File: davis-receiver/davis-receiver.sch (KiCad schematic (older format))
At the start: 150 parts, among them J1 Conn_Coaxial, J2 Wurth_74982104400, J3 JTAG, J4 UART, J5 SPI-BARO, J6 SPI-RF, Q1 FDC2512, SW1 MCU_RESET, T1 POE70P-33, U1 TM4C129ENCZADI3R, U2 CC1125RHBR, U3 FXPS7115D4, U4 TPS79930DDCR, U5 MB10S, U6 MB10S, U7 TPS23753A, U8 FOD817A3SD, U9 TLV431ACDBZR, X1 ECS-2520MV-400-AY-TR, Y1 LFXTAL071758CUTT

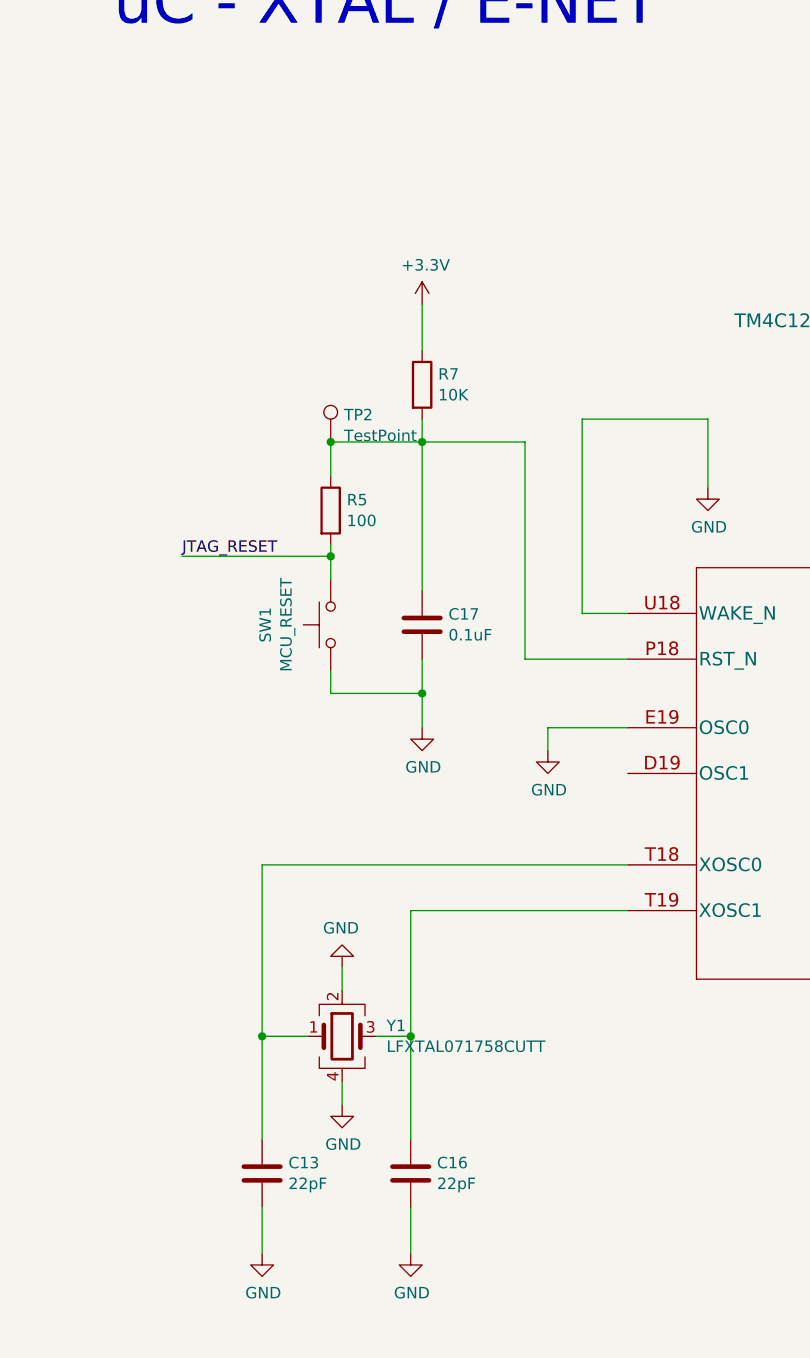
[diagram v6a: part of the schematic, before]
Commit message: Sea LED Routing Complete
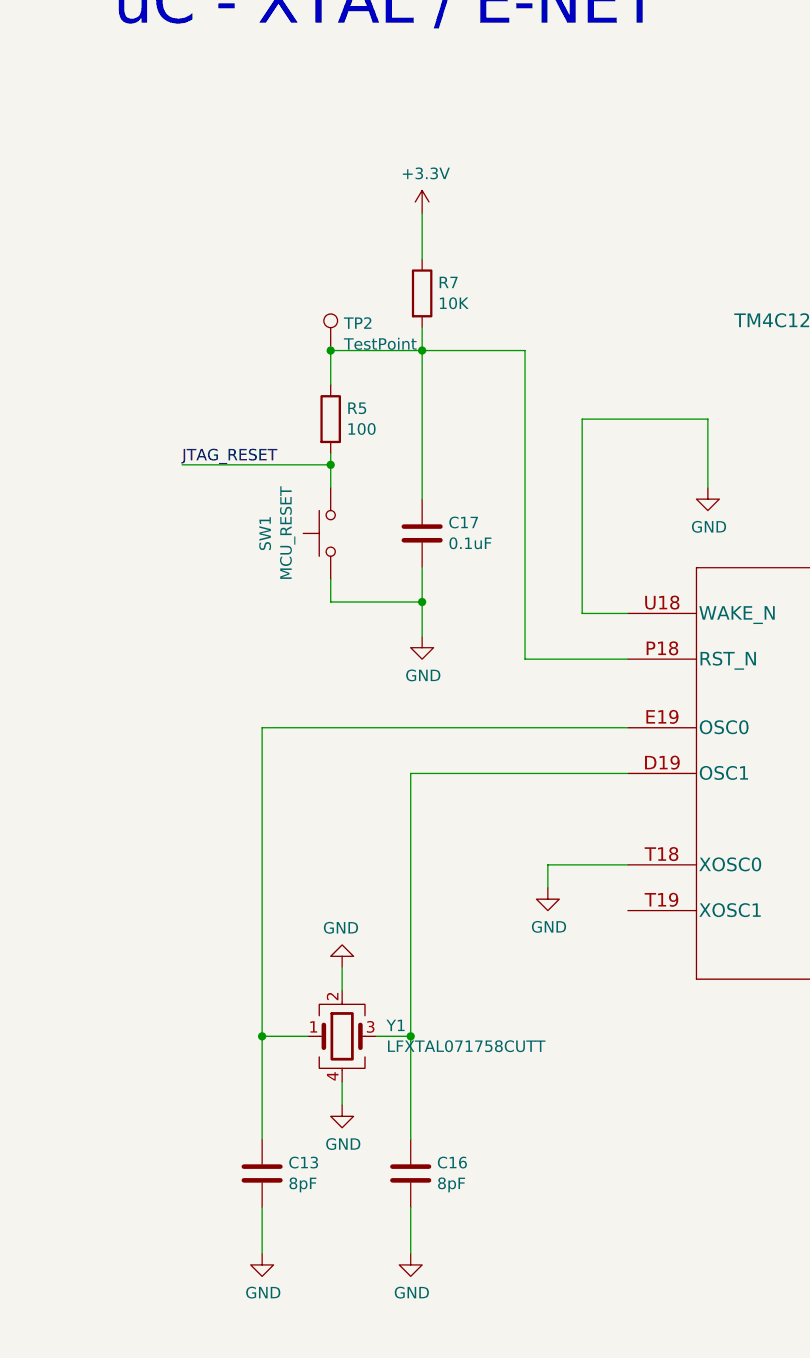
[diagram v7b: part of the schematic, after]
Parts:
- C13, C16: value 22pF -> 8pF
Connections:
- net GND: now also U1.T18 (XOSC0); no longer U1.E19 (OSC0)
- net at U1.D19 (OSC1): now also C16.1, Y1.3
- net at C13.1, Y1.1: now also U1.E19 (OSC0); no longer U1.T18 (XOSC0)
- now unconnected: U1.T19 (XOSC1)
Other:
- moved on the sheet: C17, R5, R7, SW1, TP2
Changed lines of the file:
@@
 L Switch:SW_Push SW1
 U 1 1 62515CF2
-P 10450 4100
-F 0 "SW1" H 10450 4385 50  0000 C CNN
-F 1 "MCU_RESET" H 10450 4294 50  0000 C CNN
-F 2 "Custom:PTS636" H 10450 4300 50  0001 C CNN
-F 3 "~" H 10450 4300 50  0001 C CNN
-	1    10450 4100
+P 10450 3700
+F 0 "SW1" H 10450 3985 50  0000 C CNN
+F 1 "MCU_RESET" H 10450 3894 50  0000 C CNN
+F 2 "Custom:PTS636" H 10450 3900 50  0001 C CNN
+F 3 "~" H 10450 3900 50  0001 C CNN
+	1    10450 3700
 	0    -1   -1   0
 $EndComp
@@
 L Device:R R7
 U 1 1 65AD70AF
-P 10850 3050
-F 0 "R7" H 10920 3096 50  0000 L CNN
-F 1 "10K" H 10920 3005 50  0000 L CNN
-F 2 "Resistor_SMD:R_0805_2012Metric" V 10780 3050 50  0001 C CNN
-F 3 "~" H 10850 3050 50  0001 C CNN
-	1    10850 3050
+P 10850 2650
+F 0 "R7" H 10920 2696 50  0000 L CNN
+F 1 "10K" H 10920 2605 50  0000 L CNN
+F 2 "Resistor_SMD:R_0805_2012Metric" V 10780 2650 50  0001 C CNN
+F 3 "~" H 10850 2650 50  0001 C CNN
+	1    10850 2650
 	1    0    0    -1
 $EndComp
@@
 L Device:R R5
 U 1 1 65B4A2CB
-P 10450 3600
-F 0 "R5" H 10520 3646 50  0000 L CNN
-F 1 "100" H 10520 3555 50  0000 L CNN
-F 2 "Resistor_SMD:R_0805_2012Metric" V 10380 3600 50  0001 C CNN
-F 3 "~" H 10450 3600 50  0001 C CNN
-	1    10450 3600
+P 10450 3200
+F 0 "R5" H 10520 3246 50  0000 L CNN
+F 1 "100" H 10520 3155 50  0000 L CNN
+F 2 "Resistor_SMD:R_0805_2012Metric" V 10380 3200 50  0001 C CNN
+F 3 "~" H 10450 3200 50  0001 C CNN
+	1    10450 3200
 	1    0    0    -1
 $EndComp
@@
 L Device:C C17
 U 1 1 65CA4E1B
-P 10850 4100
-F 0 "C17" H 10965 4146 50  0000 L CNN
-F 1 "0.1uF" H 10965 4055 50  0000 L CNN
-F 2 "Capacitor_SMD:C_0805_2012Metric" H 10888 3950 50  0001 C CNN
-F 3 "~" H 10850 4100 50  0001 C CNN
-	1    10850 4100
+P 10850 3700
+F 0 "C17" H 10965 3746 50  0000 L CNN
+F 1 "0.1uF" H 10965 3655 50  0000 L CNN
+F 2 "Capacitor_SMD:C_0805_2012Metric" H 10888 3550 50  0001 C CNN
+F 3 "~" H 10850 3700 50  0001 C CNN
+	1    10850 3700
 	1    0    0    -1
 $EndComp
@@
 L power:GND #PWR031
 U 1 1 65D18373
-P 10850 4550
-F 0 "#PWR031" H 10850 4300 50  0001 C CNN
-F 1 "GND" H 10855 4377 50  0000 C CNN
-F 2 "" H 10850 4550 50  0001 C CNN
-F 3 "" H 10850 4550 50  0001 C CNN
-	1    10850 4550
-	1    0    0    -1
-$EndComp
-Wire Wire Line
-	10850 3200 10850 3300
-Wire Wire Line
-	10850 3300 10450 3300
-Wire Wire Line
-	10450 3300 10450 3450
-Wire Wire Line
-	10450 4300 10450 4400
-Wire Wire Line
-	10450 4400 10850 4400
-Wire Wire Line
-	10850 4400 10850 4550
-Wire Wire Line
-	10850 4250 10850 4400
-Connection ~ 10850 4400
-Wire Wire Line
-	10850 3300 10850 3950
-Connection ~ 10850 3300
+P 10850 4150
+F 0 "#PWR031" H 10850 3900 50  0001 C CNN
+F 1 "GND" H 10855 3977 50  0000 C CNN
+F 2 "" H 10850 4150 50  0001 C CNN
+F 3 "" H 10850 4150 50  0001 C CNN
+	1    10850 4150
+	1    0    0    -1
+$EndComp
+Wire Wire Line
+	10850 2800 10850 2900
+Wire Wire Line
+	10850 2900 10450 2900
+Wire Wire Line
+	10450 2900 10450 3050
+Wire Wire Line
+	10450 3900 10450 4000
+Wire Wire Line
+	10450 4000 10850 4000
+Wire Wire Line
+	10850 4000 10850 4150
+Wire Wire Line
+	10850 3850 10850 4000
+Connection ~ 10850 4000
+Wire Wire Line
+	10850 2900 10850 3550
+Connection ~ 10850 2900
 $Comp
 L power:+3.3V #PWR030
 U 1 1 660545C2
-P 10850 2700
-F 0 "#PWR030" H 10850 2550 50  0001 C CNN
-F 1 "+3.3V" H 10865 2873 50  0000 C CNN
-F 2 "" H 10850 2700 50  0001 C CNN
-F 3 "" H 10850 2700 50  0001 C CNN
-	1    10850 2700
-	1    0    0    -1
-$EndComp
-Wire Wire Line
-	10850 2700 10850 2900
-Wire Wire Line
-	10850 3300 11300 3300
-Wire Wire Line
-	11300 3300 11300 4250
+P 10850 2300
+F 0 "#PWR030" H 10850 2150 50  0001 C CNN
+F 1 "+3.3V" H 10865 2473 50  0000 C CNN
+F 2 "" H 10850 2300 50  0001 C CNN
+F 3 "" H 10850 2300 50  0001 C CNN
+	1    10850 2300
+	1    0    0    -1
+$EndComp
+Wire Wire Line
+	10850 2300 10850 2500
+Wire Wire Line
+	10850 2900 11300 2900
 Wire Wire Line
 	11300 4250 11750 4250
@@
 P 10150 6500
 F 0 "C13" H 10265 6546 50  0000 L CNN
-F 1 "22pF" H 10265 6455 50  0000 L CNN
+F 1 "8pF" H 10265 6455 50  0000 L CNN
 F 2 "Capacitor_SMD:C_0805_2012Metric" H 10188 6350 50  0001 C CNN
 F 3 "~" H 10150 6500 50  0001 C CNN
@@
 P 10800 6500
 F 0 "C16" H 10915 6546 50  0000 L CNN
-F 1 "22pF" H 10915 6455 50  0000 L CNN
+F 1 "8pF" H 10915 6455 50  0000 L CNN
 F 2 "Capacitor_SMD:C_0805_2012Metric" H 10838 6350 50  0001 C CNN
 F 3 "~" H 10800 6500 50  0001 C CNN
@@
 $EndComp
 Wire Wire Line
-	11750 5150 10150 5150
-Wire Wire Line
-	10150 5150 10150 5900
-Wire Wire Line
 	10150 5900 10350 5900
 Connection ~ 10150 5900
@@
 	10150 5900 10150 6350
 Wire Wire Line
-	11750 5350 10800 5350
-Wire Wire Line
-	10800 5350 10800 5900
-Wire Wire Line
 	10650 5900 10800 5900
 Connection ~ 10800 5900
@@
 L power:GND #PWR036
 U 1 1 66799392
-P 11400 4650
-F 0 "#PWR036" H 11400 4400 50  0001 C CNN
-F 1 "GND" H 11405 4477 50  0000 C CNN
-F 2 "" H 11400 4650 50  0001 C CNN
-F 3 "" H 11400 4650 50  0001 C CNN
-	1    11400 4650
-	1    0    0    -1
-$EndComp
-Wire Wire Line
-	11750 4550 11400 4550
-Wire Wire Line
-	11400 4550 11400 4650
+P 11400 5250
+F 0 "#PWR036" H 11400 5000 50  0001 C CNN
+F 1 "GND" H 11405 5077 50  0000 C CNN
+F 2 "" H 11400 5250 50  0001 C CNN
+F 3 "" H 11400 5250 50  0001 C CNN
+	1    11400 5250
+	1    0    0    -1
+$EndComp
+Wire Wire Line
+	11750 5150 11400 5150
+Wire Wire Line
+	11400 5150 11400 5250
 $Comp
 L power:GND #PWR027
@@
 Wire Wire Line
 	18650 19550 18750 19550
-Text Label 9800 3800 0    50   ~ 0
+Text Label 9800 3400 0    50   ~ 0
 JTAG_RESET
 Wire Wire Line
-	9800 3800 10450 3800
-Wire Wire Line
-	10450 3750 10450 3800
-Connection ~ 10450 3800
-Wire Wire Line
-	10450 3800 10450 3900
+	9800 3400 10450 3400
+Wire Wire Line
+	10450 3350 10450 3400
+Connection ~ 10450 3400
+Wire Wire Line
+	10450 3400 10450 3500
 Text Label 1800 4000 0    50   ~ 0
 JTAG_TCK
@@
 L Connector:TestPoint TP2
 U 1 1 6410086E
-P 10450 3300
-F 0 "TP2" H 10508 3418 50  0000 L CNN
-F 1 "TestPoint" H 10508 3327 50  0000 L CNN
-F 2 "TestPoint:TestPoint_Pad_D2.0mm" H 10650 3300 50  0001 C CNN
-F 3 "~" H 10650 3300 50  0001 C CNN
-	1    10450 3300
+P 10450 2900
+F 0 "TP2" H 10508 3018 50  0000 L CNN
+F 1 "TestPoint" H 10508 2927 50  0000 L CNN
+F 2 "TestPoint:TestPoint_Pad_D2.0mm" H 10650 2900 50  0001 C CNN
+F 3 "~" H 10650 2900 50  0001 C CNN
+	1    10450 2900
 	1    0    0    -1
 $EndComp
@@
 Text Notes 17000 18500 0    197  ~ 0
 JTAG / Debug Conns
-Connection ~ 10450 3300
+Connection ~ 10450 2900
 $Comp
 L Connector:TestPoint TP3
@@
 	15300 6000 15600 6000
 Connection ~ 15600 6000
+Wire Wire Line
+	11300 2900 11300 4250
+Wire Wire Line
+	11750 4550 10150 4550
+Wire Wire Line
+	10150 4550 10150 5900
+Wire Wire Line
+	10800 4750 11750 4750
+Wire Wire Line
+	10800 4750 10800 5900
 $EndSCHEMATC

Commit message: Updates to DavisReceiver
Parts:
- removed TP2: TestPoint, TestPoint:TestPoint_Pad_D2.0mm, symbol Connector:TestPoint
- added D7: LED, LED_SMD:LED_1206_3216Metric, symbol Device:LED
- added J7: GPIO-RF, Custom:TC2030-IDC-FP, symbol Custom:TC2030-GPIO
- added R31: 100, Resistor_SMD:R_0805_2012Metric, symbol Device:R
- added TP12: TestPoint, TestPoint:TestPoint_Pad_D1.0mm, symbol Connector:TestPoint
- C1, C2, C39, C49, C54, C55, C56, C58, C59, C60, C62, C63, C64, C66, C67, C68: value 0.1uF -> 100n
- C10: value 2.2uF -> 2u2
- C11, C12, C22, C25, C28, C3, C31, C32, C5, C8: value 0.047uF -> 47n
- C18: value 33pF -> 33p
- C19, C47: value 100pF -> 100p
- C20: value 15pF -> 15p
- C21: value 10nF -> 10n
- C23, C26: value 3.3pF -> 3p3
- C24, C38: value 47nF -> 47n
- C27: value 1pF -> 1p
- C29: value 1.8nF -> 1n8
- C30: value 2.2pF -> 2p2
- C33: value 3pF -> 3p
- C34: value 22uF 63V -> 22u 63V
- C36: value 1uF 100V -> 1u 100V
- C4: value 220nF -> 220n
- C40: value 0.22uF -> 220n
- C42: value 10nF 100V -> 10n 100V
- C43: value 10uF -> 10u
- C46, C48: value 1uF -> 1u
- C50: value 01.uF -> 100n
- C51: value 47uf -> 47u
- C52: value 11900pF -> 11n9
- C53, C57: value 47uF -> 47u
- C6: value 22pF -> 22p
- C9: value 0.01uF -> 10n
- D1: footprint LED_SMD:LED_Cree-PLCC4_2x2mm_CW -> LED_SMD:LED_Cree-PLCC4_3.2x2.8mm_CCW; symbol Custom:LED_ABGR -> Device:LED_RABG
- L2: value 15nH -> 15n
- L3, L4, L6, L8: value 12nH -> 12n
- L5: value 7.5nH -> 7n5
- L7: value 18nH -> 18n
- L9: value 4.7uH SDR7030 -> 4u7 SDR7030
- R10: value 1.27K -> 1k27
- R11: value 24.9K -> 24k9
- R18: value 80K 0.1W -> 80k 0.1W
- R19: value 2K -> 2k
- R26: value 10K -> 10k
- R27: value 7.15K -> 7k15
- R28: value 41.2K -> 41k2
- R29: value 24.3K -> 24k3
- R4: value 56K -> 56k
- R8: value 59.0K -> 59k
- R9: value 80.6K -> 80k6
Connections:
- net +3V3: now also D1.2 (A), J3.1 (VCC), D7.1 (K); no longer D1.1 (A)
- net GND: now also J7.1, R31.2
- net IND_G: now also R2.2; no longer R1.2
- net IND_R: now also R1.2; no longer R2.2
- net RF_GPIO0: now also J7.2
- net RF_GPIO2: now also J7.3
- net RF_GPIO3: now also J7.4
- net at C17.1, R7.2, U1.P18 (RST_N): now also R5.2; no longer R5.1
- net DIVSCLK: now reaches U1.A13 (PQ4)
- net DIVSCLK: now also TP12.1
- net at R3.1: now also D1.3 (BK); no longer D1.2 (BK)
- net at R1.1: now also D1.1 (RK); no longer D1.3 (GK)
- net at TP5.1, U7.1 (CTL), U8.4: now also C38.1, R19.2; no longer C38.2, R19.1
- net at C39.1, TP8.1, U7.2 (Vb): now also R14.1, R19.1; no longer R14.2, R19.2
- net VSS_POE: now reaches C14.2, D2.2, R10.2, TP4.1, U5.2 (NEG), U6.2 (NEG), U7.7 (VSS)
- net JTAG_RESET renamed ~JTAG_RESET~
- net ~JTAG_RESET~: now also R5.1; no longer R5.2
- new net: C38.2, R14.2
- new net: D7.2 (A), R31.1
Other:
- note added: "HMI"
- note added: "High Voltage (Isolated)"
- note added: "Low Voltage (Isolated)"
- note added: "RF POWER"
- note added: "uC - AUX. / ETHERNET"
- note added: "uC Power / Decouple"
- note removed: "uC - XTAL / E-NET"
- note removed: "uC Power"
- moved on the sheet: C1, C10, C11, C12, C13, C14, C15, C16, C17, C18, C19, C2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
